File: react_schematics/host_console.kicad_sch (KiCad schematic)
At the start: 8 parts, among them J3 RJ45_Shielded, U6 12-24_buck_1, U7 MAX485E

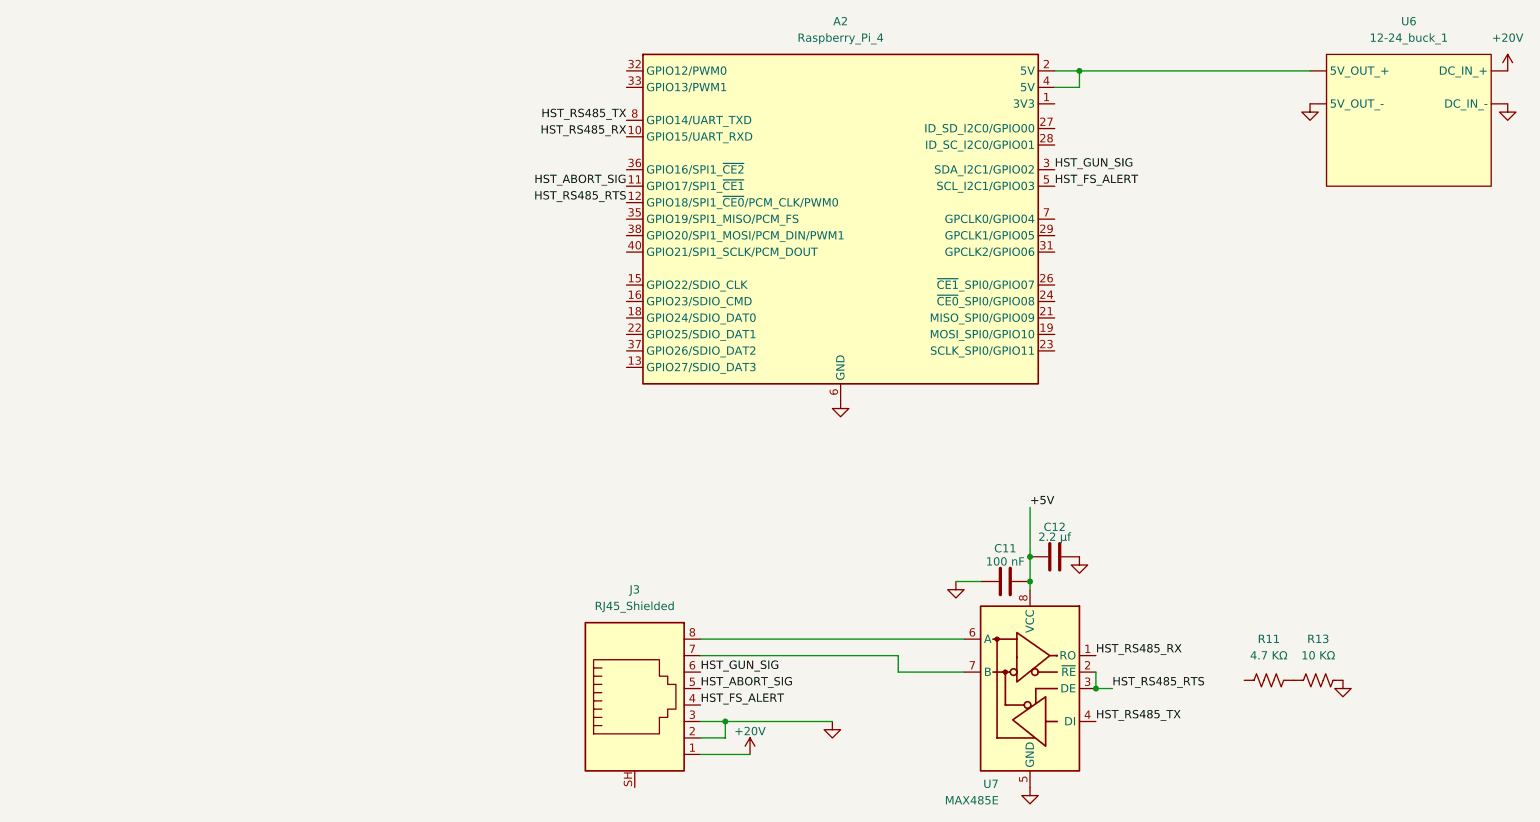
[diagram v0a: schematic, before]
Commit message: rs485 mode finally enabled
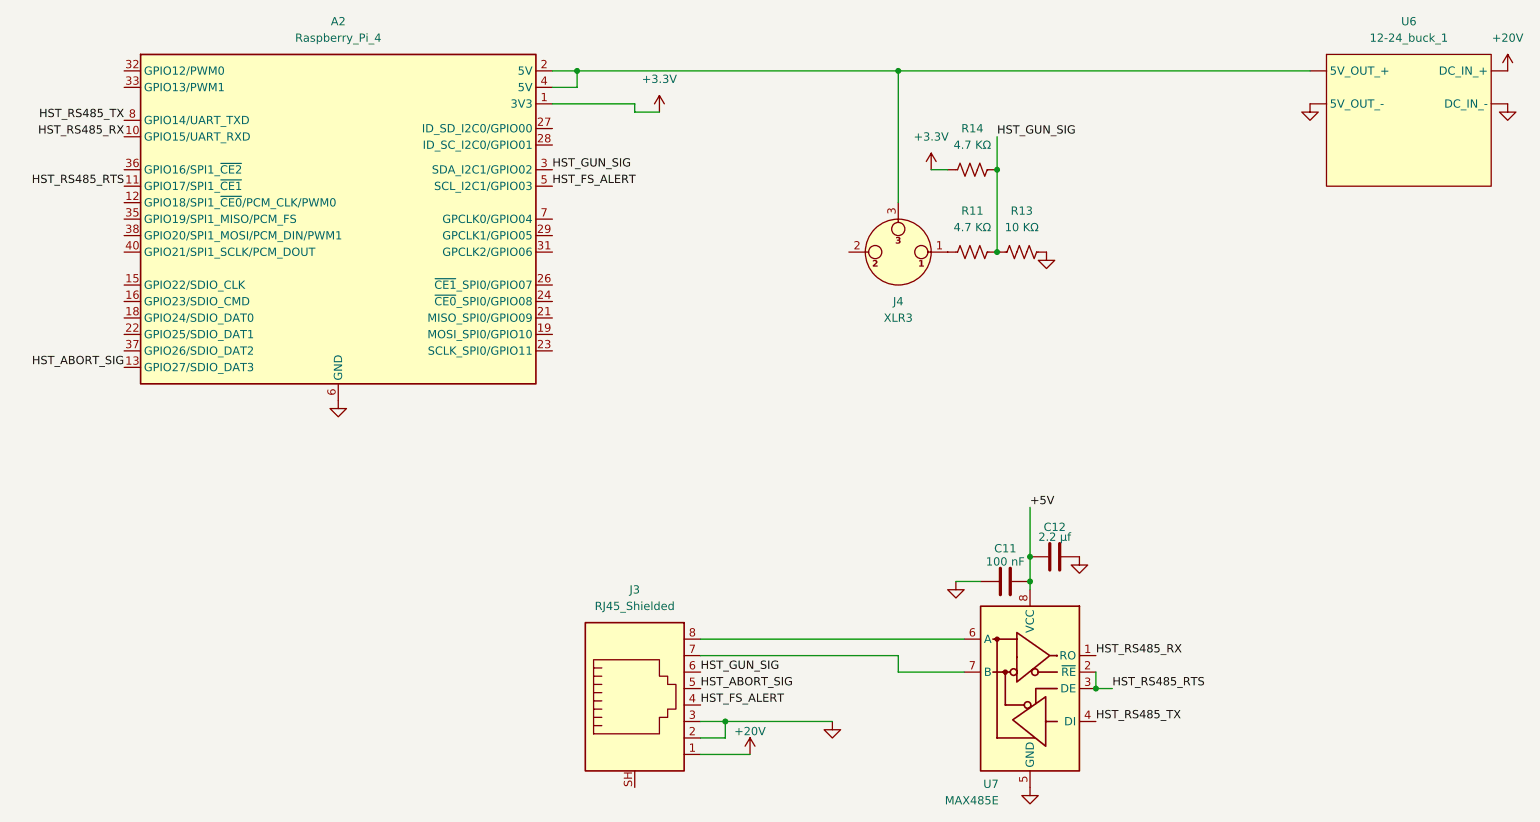
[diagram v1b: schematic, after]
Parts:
- added J4: XLR3, symbol Connector_Audio:XLR3
- added R14: 4.7 KΩ, symbol Device:R_US
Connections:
- net HST_ABORT_SIG: now also A2.13 (GPIO27/SDIO_DAT3); no longer A2.11 (GPIO17/SPI1_~{CE1})
- net HST_GUN_SIG: now also R11.1, R13.2, R14.1
- net HST_RS485_RTS: now also A2.11 (GPIO17/SPI1_~{CE1}); no longer A2.12 (GPIO18/SPI1_~{CE0}/PCM_CLK/PWM0)
- net at R11.2: now also J4.1
- net +3.3V: now reaches A2.1 (3V3)
- net +3.3V: now also R14.2
- net at A2.17 (3V3), A2.2 (5V), A2.4 (5V)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: now also J4.3
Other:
- moved on the sheet: A2, R11, R13

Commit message: uh-oh wah wahs
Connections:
- net HST_FS_ALERT: now also A2.7 (GPCLK0/GPIO04); no longer A2.5 (SCL_I2C1/GPIO03)
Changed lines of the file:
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@@
 	)
 	(label "HST_FS_ALERT"
-		(at 96.52 44.45 0)
+		(at 96.52 49.53 0)
 		(effects
 			(font
